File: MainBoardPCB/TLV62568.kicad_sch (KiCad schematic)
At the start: 7 parts, among them U2 TLV62568DDC

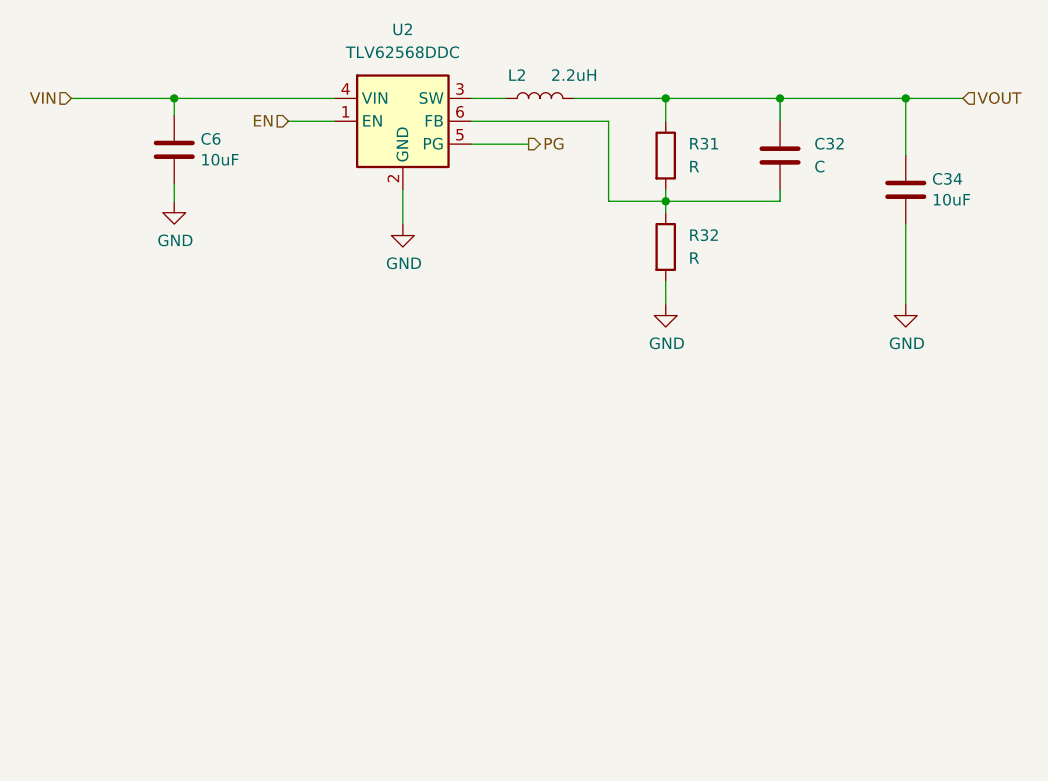
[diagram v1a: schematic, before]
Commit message: New Fusion main board version using a more beefy MCU.
Signed-off-by: Alexis Jeandet <alexis.jeandet@member.fsf.org>
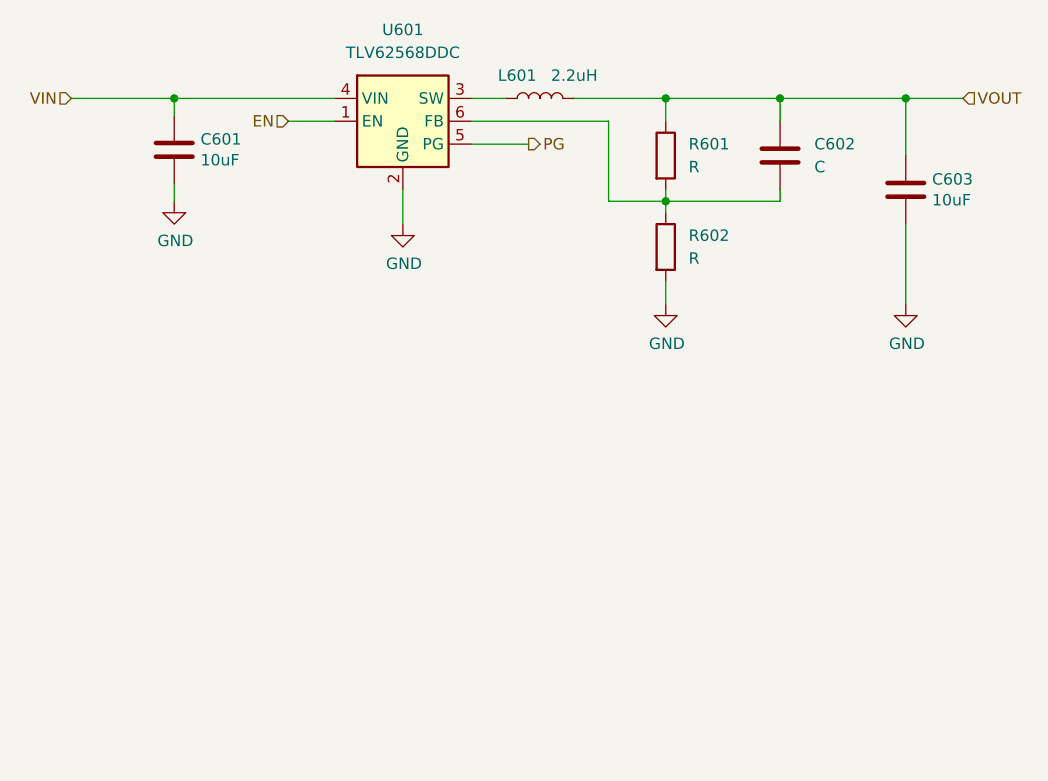
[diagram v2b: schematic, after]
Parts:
- renumbered C6 to C601, C32 to C602, C34 to C603, L2 to L601, R31 to R601, R32 to R602, U2 to U601
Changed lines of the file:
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@@
 (kicad_sch
-	(version 20231120)
+	(version 20250114)
 	(generator "eeschema")
-	(generator_version "8.0")
+	(generator_version "9.0")
 	(paper "A4")
 	(title_block
 		(title "Fusion")
-		(date "2024-03-15")
-		(rev "1.0")
+		(date "2025-05-30")
+		(rev "2.0")
 		(company "LPP/CNRS")
 		(comment 1 "Alexis Jeandet")
@@
 			"5nCfgTyMMWFgYGBgaDASlzWYgYGBgUH6YIwJAwMDA0ODYYwJAwMDA0ODYYwJAwMDA0ODYYwJAwMD"
 			"A0ODYQNg0mQyMDAwMDSEzxwAqQCcAaiLWRkGBgYGBunjM4DF/wdHJaXS6QNS2AAAAABJRU5ErkJg"
-			"gg=="
+			"ggAAAAAAAAAAAAAAAAAAAAAAAAAAAAAAAAAAAAAAAAAAAAAAAAAAAAAAAAAAAAAAAAAAAAAAAAAA"
+			"AAAAAAAAAAAAAAAAAAAAAAAAAAAAAAAAAAAAAAAAAAAAAAAAAAAAAAAAAAAAAAAAAAAAAAAAAAAA"
+			"AAAAAAAAAAAAAAAAAAAAAAAAAAAAAAAAAAAAAAAAAAAAAAAAAAAAAAAAAAAAAAAAAAAAAAAAAAAA"
+			"AAAAAAAAAAAAAAAAAAAAAAAAAAAAAAAAAAAAAAAAAAAAAAAAAAAAAAAAAAAAAAAAAAAAAAAAAAAA"
+			"AAAAAAAAAAAAAAAAAAAAAAAAAAAAAAAAAAAAAAAAAAAAAAAAAAAAAAAAAAAAAAAAAAAAAAAAAAAA"
+			"AAAAAAAAAAAAAAAAAAAAAAAAAAAAAAAAAAAAAAAAAAAAAAAAAAAAAAAAAAAAAAAAAAAAAAAAAAAA"
+			"AAAAAAAAAAAAAAAAAAAAAAAAAAAAAAAAAAAAAAAAAAAAAAAAAAAAAAAAAAAAAAAAAAAAAAAAAAAA"
+			"AAAAAAAAAAAAAAAAAAAAAAAAAAAAAAAAAAAAAAAAAAAAAAAAAAAAAAAAAAAAAAAAAAAAAAAAAAAA"
+			"AAAAAAAAAAAAAAAAAAAAAAAAAAAAAAAAAAAAAAAAAAAAAAAAAAAAAAAAAAAAAAAAAAAAAAAAAAAA"
+			"AAAAAAAAAAAAAAAAAAAAAAAAAAAAAAAAAAAAAAAAAAAAAAAAAAAAAAAAAAAAAAAAAAAAAAAAAAAA"
+			"AAAAAAAAAAAAAAAAAAAAAAAAAAAAAAAAAAAAAAAAAAAAAAAAAAAAAAAAAAAAAAAAAAAAAAAAAAAA"
+			"AAAAAAAAAAAAAAAAAAAAAAAAAAAAAAAAAAAAAAAAAAAAAAAAAAAAAAAAAAAAAAAAAAAAAAAAAAAA"
+			"AAAAAAAAAAAAAAAAAAAAAAAAAAAAAAAAAAAAAAAAAAAAAAAAAAAAAAAAAAAAAAAAAAAAAAAAAAAA"
+			"AAAAAAAAAAAAAAAAAAAAAAAAAAAAAAAAAAAAAAAAAAAAAAAAAAAAAAAAAAAAAAAAAAAAAAAAAAAA"
+			"AAAAAAAAAAAAAAAAAAAAAAAAAAAAAAAAAAAAAAAAAAAAAAAAAAAAAAAAAAAAAAAAAAAAAAAAAAAA"
+			"AAAAAAAAAAAAAAAAAAAAAAAAAAAAAAAAAAAAAAAAAAAAAAAAAAAAAAAAAAAAAAAAAAAAAAAAAAAA"
+			"AAAAAAAAAAAAAAAAAAAAAAAAAAAAAAAAAAAAAAAAAAAAAAAAAAAAAAAAAAAAAAAAAAAAAAAAAAAA"
+			"AAAAAAAAAAAAAAAAAAAAAAAAAAAAAAAAAAAAAAAAAAAAAAAAAAAAAAAAAAAAAAAAAAAAAAAAAAAA"
+			"AA=="
 		)
 	)
@@
 		(shape input)
 		(at 177.8 77.47 0)
-		(fields_autoplaced yes)
 		(effects
 			(font
@@
 		(shape input)
 		(at 78.74 77.47 180)
-		(fields_autoplaced yes)
 		(effects
 			(font
@@
 		(shape input)
 		(at 102.87 80.01 180)
-		(fields_autoplaced yes)
 		(effects
 			(font
@@
 		(shape output)
 		(at 129.54 82.55 0)
-		(fields_autoplaced yes)
 		(effects
 			(font
@@
 		(on_board yes)
 		(dnp no)
-		(property "Reference" "L2"
+		(property "Reference" "L601"
 			(at 128.27 74.93 90)
 			(effects
@@
 			(project "Fusion"
 				(path "/9f566196-80c5-4736-8658-8706a05587fc/62990c39-da3d-4c4d-9a99-7726d3081efd/3002c500-aed7-4176-86ba-91e660fbab71"
-					(reference "L2")
+					(reference "L601")
 					(unit 1)
 				)
 				(path "/9f566196-80c5-4736-8658-8706a05587fc/62990c39-da3d-4c4d-9a99-7726d3081efd/4840b69f-93f4-42ce-9914-822d0705bea2"
-					(reference "L3")
+					(reference "L701")
 					(unit 1)
 				)
@@
 		(dnp no)
 		(fields_autoplaced yes)
-		(property "Reference" "R31"
+		(property "Reference" "R601"
 			(at 147.32 82.55 0)
 			(effects
@@
 			(project "Fusion"
 				(path "/9f566196-80c5-4736-8658-8706a05587fc/62990c39-da3d-4c4d-9a99-7726d3081efd/3002c500-aed7-4176-86ba-91e660fbab71"
-					(reference "R31")
+					(reference "R601")
 					(unit 1)
 				)
 				(path "/9f566196-80c5-4736-8658-8706a05587fc/62990c39-da3d-4c4d-9a99-7726d3081efd/4840b69f-93f4-42ce-9914-822d0705bea2"
-					(reference "R30")
+					(reference "R701")
 					(unit 1)
 				)
@@
 		(on_board yes)
 		(dnp no)
-		(property "Reference" "C34"
+		(property "Reference" "C603"
 			(at 174.371 86.4616 0)
 			(effects
@@
 			(project "Fusion"
 				(path "/9f566196-80c5-4736-8658-8706a05587fc/62990c39-da3d-4c4d-9a99-7726d3081efd/3002c500-aed7-4176-86ba-91e660fbab71"
-					(reference "C34")
+					(reference "C603")
 					(unit 1)
 				)
 				(path "/9f566196-80c5-4736-8658-8706a05587fc/62990c39-da3d-4c4d-9a99-7726d3081efd/4840b69f-93f4-42ce-9914-822d0705bea2"
-					(reference "C40")
+					(reference "C703")
 					(unit 1)
 				)
@@
 		(on_board yes)
 		(dnp no)
-		(property "Reference" "#PWR050"
+		(property "Reference" "#PWR0603"
 			(at 144.78 106.68 0)
 			(effects
@@
 			(project "Fusion"
 				(path "/9f566196-80c5-4736-8658-8706a05587fc/62990c39-da3d-4c4d-9a99-7726d3081efd/3002c500-aed7-4176-86ba-91e660fbab71"
-					(reference "#PWR050")
+					(reference "#PWR0603")
 					(unit 1)
 				)
 				(path "/9f566196-80c5-4736-8658-8706a05587fc/62990c39-da3d-4c4d-9a99-7726d3081efd/4840b69f-93f4-42ce-9914-822d0705bea2"
-					(reference "#PWR055")
+					(reference "#PWR0703")
 					(unit 1)
 				)
@@
 		(dnp no)
 		(fields_autoplaced yes)
-		(property "Reference" "R32"
+		(property "Reference" "R602"
 			(at 147.32 92.71 0)
 			(effects
@@
 			(project "Fusion"
 				(path "/9f566196-80c5-4736-8658-8706a05587fc/62990c39-da3d-4c4d-9a99-7726d3081efd/3002c500-aed7-4176-86ba-91e660fbab71"
-					(reference "R32")
+					(reference "R602")
 					(unit 1)
 				)
 				(path "/9f566196-80c5-4736-8658-8706a05587fc/62990c39-da3d-4c4d-9a99-7726d3081efd/4840b69f-93f4-42ce-9914-822d0705bea2"
-					(reference "R33")
+					(reference "R702")
 					(unit 1)
 				)
@@
 		(on_board yes)
 		(dnp no)
-		(property "Reference" "#PWR048"
+		(property "Reference" "#PWR0602"
 			(at 115.57 97.79 0)
 			(effects
@@
 			(project "Fusion"
 				(path "/9f566196-80c5-4736-8658-8706a05587fc/62990c39-da3d-4c4d-9a99-7726d3081efd/3002c500-aed7-4176-86ba-91e660fbab71"
-					(reference "#PWR048")
+					(reference "#PWR0602")
 					(unit 1)
 				)
 				(path "/9f566196-80c5-4736-8658-8706a05587fc/62990c39-da3d-4c4d-9a99-7726d3081efd/4840b69f-93f4-42ce-9914-822d0705bea2"
-					(reference "#PWR053")
+					(reference "#PWR0702")
 					(unit 1)
 				)
@@
 		(on_board yes)
 		(dnp no)
-		(property "Reference" "#PWR043"
+		(property "Reference" "#PWR0601"
 			(at 90.17 95.25 0)
 			(effects
@@
 			(project "Fusion"
 				(path "/9f566196-80c5-4736-8658-8706a05587fc/62990c39-da3d-4c4d-9a99-7726d3081efd/3002c500-aed7-4176-86ba-91e660fbab71"
-					(reference "#PWR043")
+					(reference "#PWR0601")
 					(unit 1)
 				)
 				(path "/9f566196-80c5-4736-8658-8706a05587fc/62990c39-da3d-4c4d-9a99-7726d3081efd/4840b69f-93f4-42ce-9914-822d0705bea2"
-					(reference "#PWR052")
+					(reference "#PWR0701")
 					(unit 1)
 				)
@@
 		(on_board yes)
 		(dnp no)
-		(property "Reference" "#PWR051"
+		(property "Reference" "#PWR0604"
 			(at 171.45 106.68 0)
 			(effects
@@
 			(project "Fusion"
 				(path "/9f566196-80c5-4736-8658-8706a05587fc/62990c39-da3d-4c4d-9a99-7726d3081efd/3002c500-aed7-4176-86ba-91e660fbab71"
-					(reference "#PWR051")
+					(reference "#PWR0604")
 					(unit 1)
 				)
 				(path "/9f566196-80c5-4736-8658-8706a05587fc/62990c39-da3d-4c4d-9a99-7726d3081efd/4840b69f-93f4-42ce-9914-822d0705bea2"
-					(reference "#PWR056")
+					(reference "#PWR0704")
 					(unit 1)
 				)
@@
 		(dnp no)
 		(fields_autoplaced yes)
-		(property "Reference" "U2"
+		(property "Reference" "U601"
 			(at 115.57 69.85 0)
 			(effects
@@
 			(project "Fusion"
 				(path "/9f566196-80c5-4736-8658-8706a05587fc/62990c39-da3d-4c4d-9a99-7726d3081efd/3002c500-aed7-4176-86ba-91e660fbab71"
-					(reference "U2")
+					(reference "U601")
 					(unit 1)
 				)
 				(path "/9f566196-80c5-4736-8658-8706a05587fc/62990c39-da3d-4c4d-9a99-7726d3081efd/4840b69f-93f4-42ce-9914-822d0705bea2"
-					(reference "U9")
+					(reference "U701")
 					(unit 1)
 				)
@@
 		(on_board yes)
 		(dnp no)
-		(property "Reference" "C6"
+		(property "Reference" "C601"
 			(at 93.091 82.0166 0)
 			(effects
@@
 			(project "Fusion"
 				(path "/9f566196-80c5-4736-8658-8706a05587fc/62990c39-da3d-4c4d-9a99-7726d3081efd/3002c500-aed7-4176-86ba-91e660fbab71"
-					(reference "C6")
+					(reference "C601")
 					(unit 1)
 				)
 				(path "/9f566196-80c5-4736-8658-8706a05587fc/62990c39-da3d-4c4d-9a99-7726d3081efd/4840b69f-93f4-42ce-9914-822d0705bea2"
-					(reference "C38")
+					(reference "C701")
 					(unit 1)
 				)
@@
 		(dnp no)
 		(fields_autoplaced yes)
-		(property "Reference" "C32"
+		(property "Reference" "C602"
 			(at 161.29 82.55 0)
 			(effects
@@
 			(project "Fusion"
 				(path "/9f566196-80c5-4736-8658-8706a05587fc/62990c39-da3d-4c4d-9a99-7726d3081efd/3002c500-aed7-4176-86ba-91e660fbab71"
-					(reference "C32")
+					(reference "C602")
 					(unit 1)
 				)
 				(path "/9f566196-80c5-4736-8658-8706a05587fc/62990c39-da3d-4c4d-9a99-7726d3081efd/4840b69f-93f4-42ce-9914-822d0705bea2"
-					(reference "C39")
-					(unit 1)
-				)
+					(reference "C702")
+					(unit 1)
+				)

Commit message: New FPGA only version
Signed-off-by: Alexis Jeandet <alexis.jeandet@member.fsf.org>
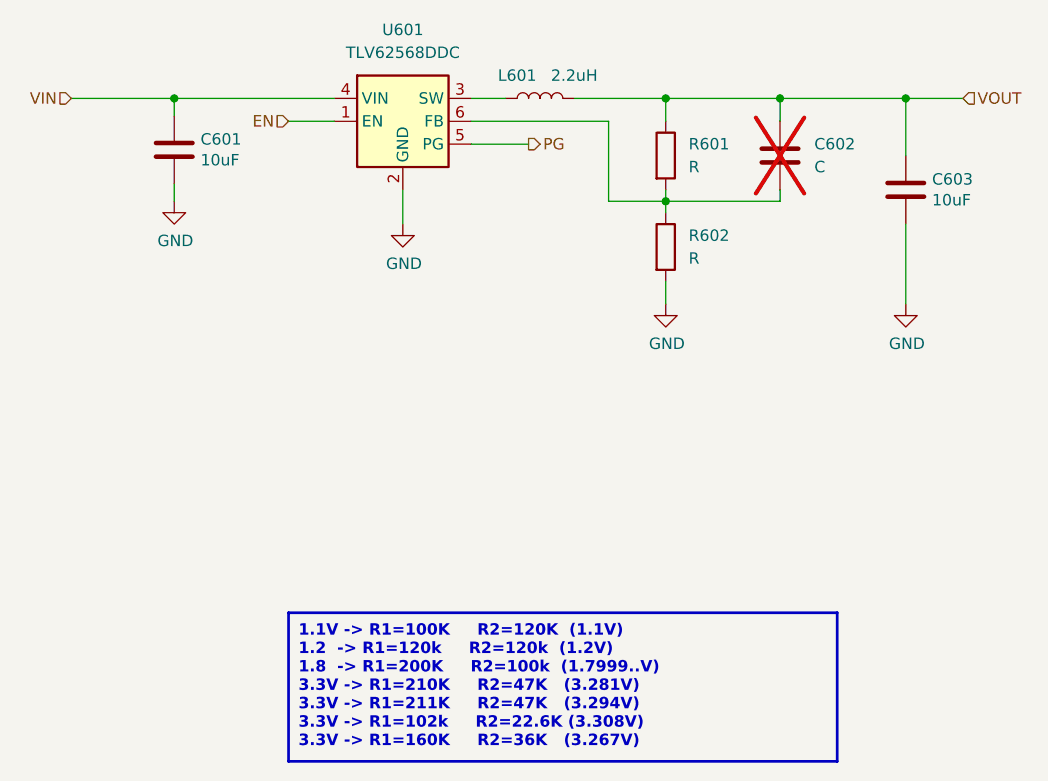
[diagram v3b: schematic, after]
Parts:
- C602: now not fitted
